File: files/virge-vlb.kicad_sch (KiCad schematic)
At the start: 45 parts, among them J2 VGA, J3 VESA feature, U1 86C325, Y1 14.318MHz

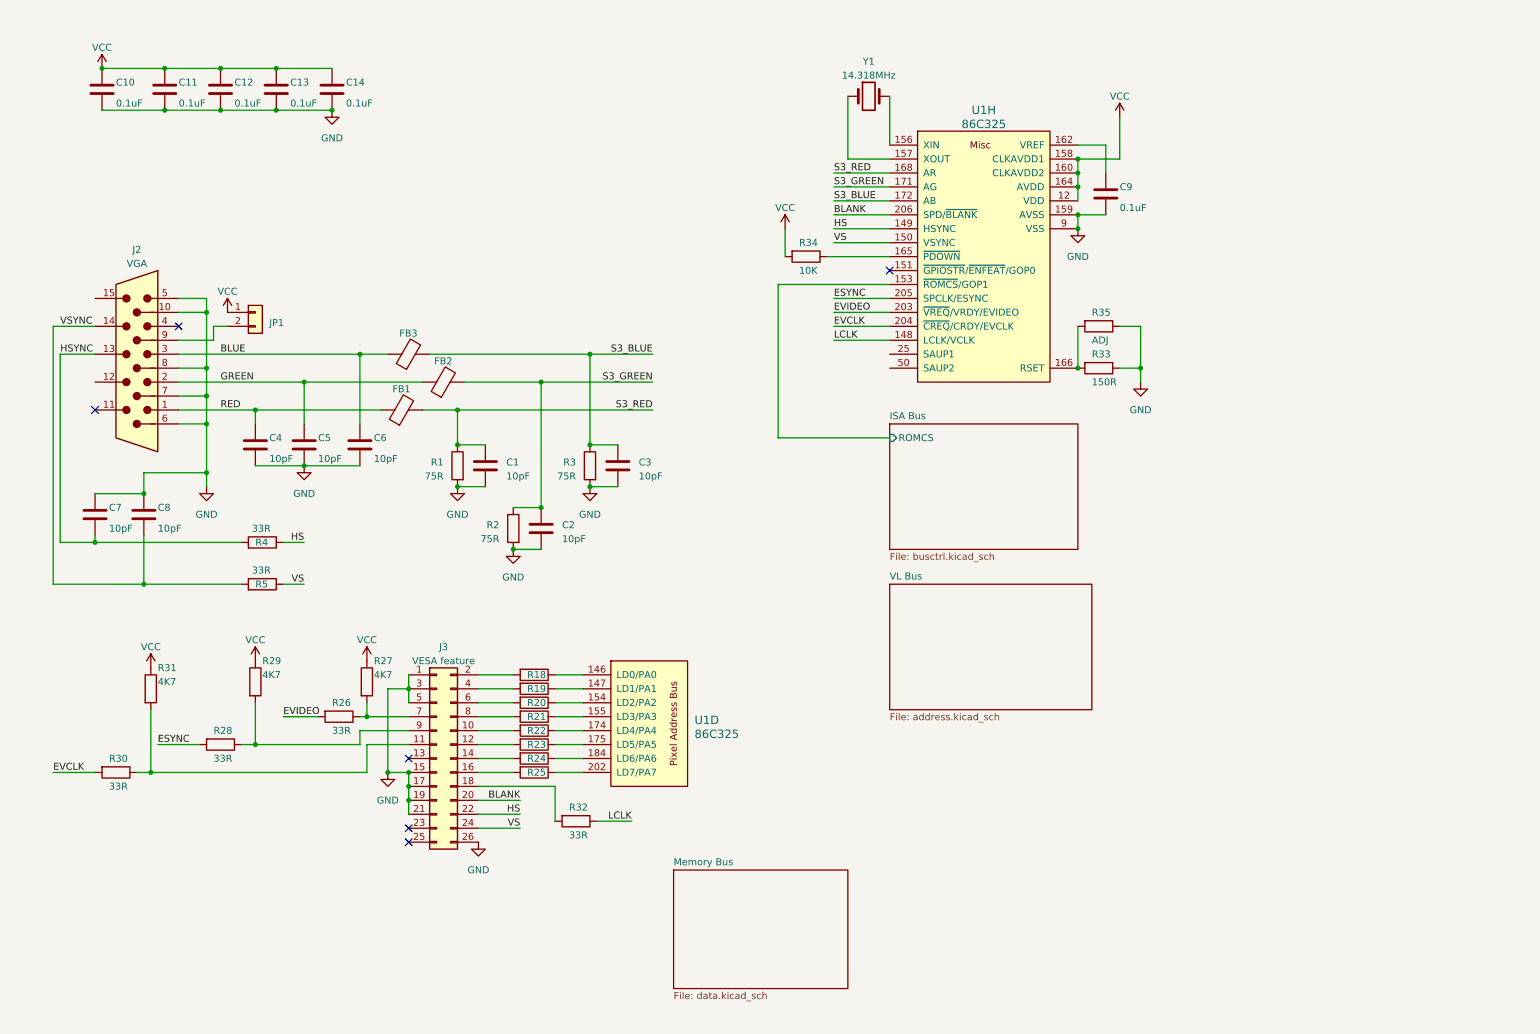
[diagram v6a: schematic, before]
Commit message: added SAUP decoding, adjusted VGA conn.
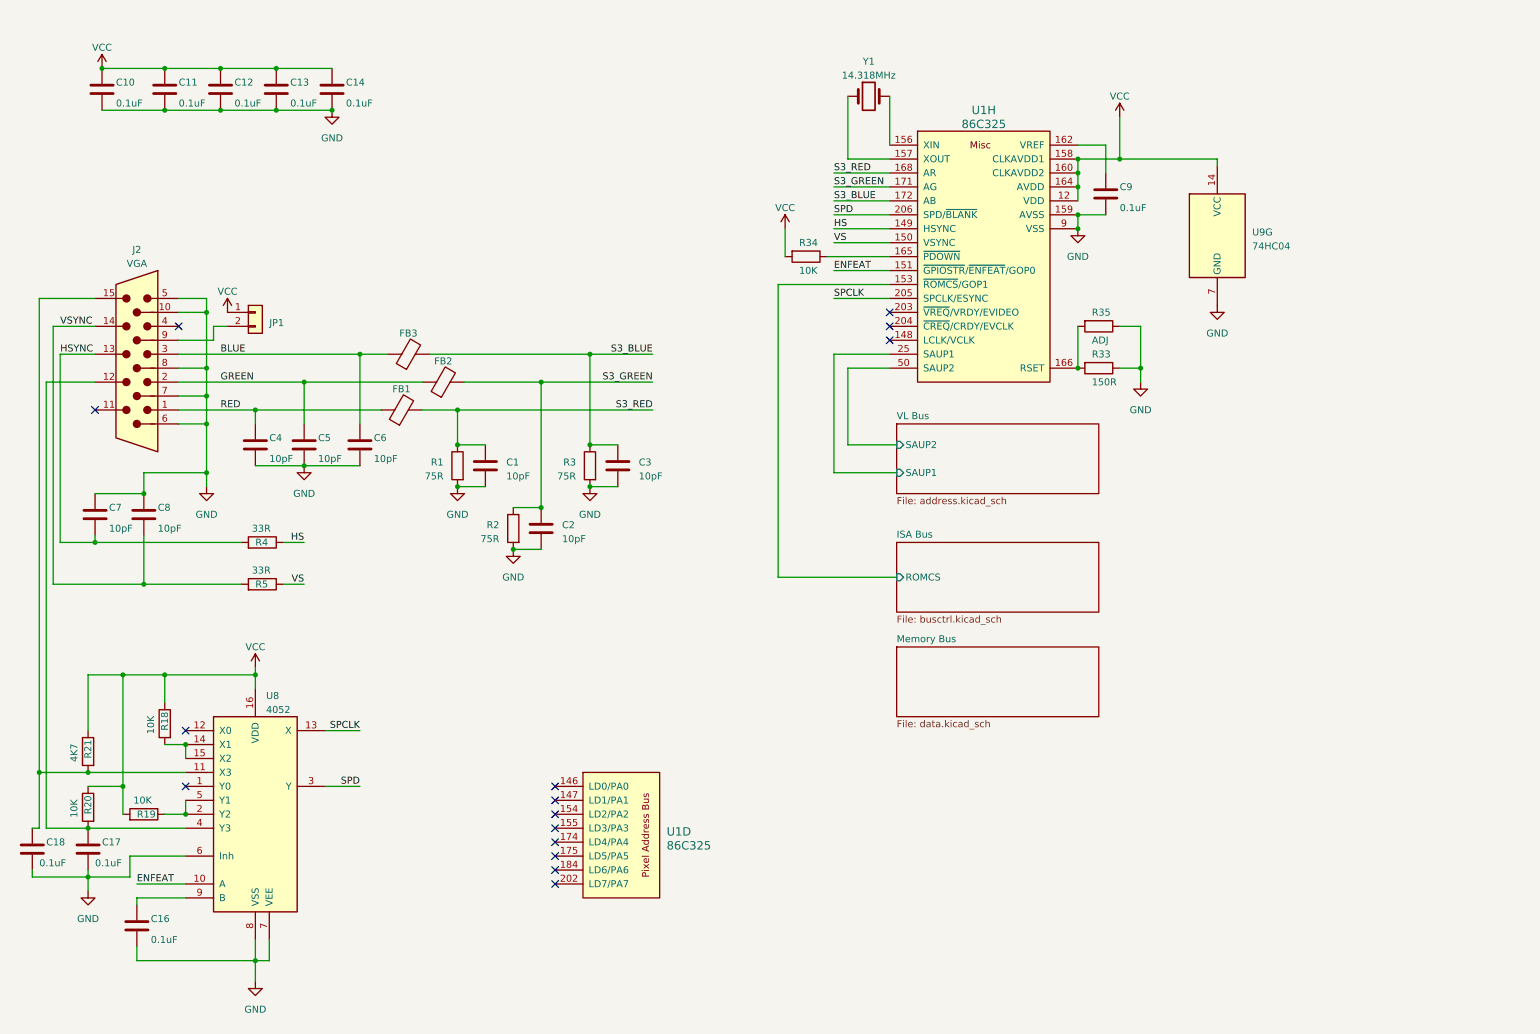
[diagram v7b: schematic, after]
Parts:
- removed J3: VESA feature, Connector_PinHeader_2.54mm:PinHeader_2x13_P2.54mm_Vertical, symbol Connector_Generic:Conn_02x13_Odd_Even
- removed R22, R23, R24, R25, R26, R28, R30, R32: 33R, Resistor_SMD:R_0805_2012Metric_Pad1.20x1.40mm_HandSolder, symbol Device:R
- removed R27, R29, R31: 4K7, Resistor_SMD:R_0805_2012Metric_Pad1.20x1.40mm_HandSolder, symbol Device:R
- added C16, C17, C18: 0.1uF, Capacitor_SMD:C_0805_2012Metric_Pad1.18x1.45mm_HandSolder, symbol Device:C
- added U8: 4052, Package_SO:SO-16_3.9x9.9mm_P1.27mm, symbol 4xxx:4052
- added U9: 74HC04, Package_SO:SO-14_3.9x8.65mm_P1.27mm, symbol 74xx:74HC04
- R18, R19, R20: value 33R -> 10K
- R21: value 33R -> 4K7
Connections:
- net GND: now also C16.2, C17.2, C18.2, U8.6 (Inh), U8.7 (VEE), U8.8 (VSS), U9.7 (GND)
- net VCC: now also R18.1, R19.2, R20.1, R21.1, U8.16 (VDD), U9.14 (VCC)
- net at U1.146 (LD0/PA0): no longer R18.1
- net at U1.147 (LD1/PA1): no longer R19.1
- net at U1.154 (LD2/PA2): no longer R20.1
- net at U1.155 (LD3/PA3): no longer R21.1
- net at R18.2: now also U8.14 (X1), U8.15 (X2)
- net at R20.2: now also J2.12, C17.1, U8.4 (Y3)
- net at R21.2: now also J2.15, C18.1, U8.11 (X3)
- net ENFEAT: now reaches U1.151 (~{GPIOSTR}/~{ENFEAT}/GOP0)
- net ENFEAT: now also U8.10 (A)
- net VL Bus/SAUP1: now reaches U1.25 (SAUP1)
- net VL Bus/SAUP2: now reaches U1.50 (SAUP2)
- net BLANK renamed SPD
- net SPD: now also U8.3 (Y)
- net ESYNC renamed SPCLK
- net SPCLK: now also U8.13 (X)
- net EVCLK: no longer names the net of U1.204 (~{CREQ}/CRDY/EVCLK)
- net EVIDEO: no longer names the net of U1.203 (~{VREQ}/VRDY/EVIDEO)
- net LCLK: no longer names the net of U1.148 (LCLK/VCLK)
- new net: R19.1, U8.2 (Y2), U8.5 (Y1)
- new net: C16.1, U8.9 (B)
- no-connect marks 6 -> 15
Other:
- sheet VL Bus ports: added SAUP1, SAUP2; removed none
- moved on the sheet: U1D

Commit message: added address jumpers
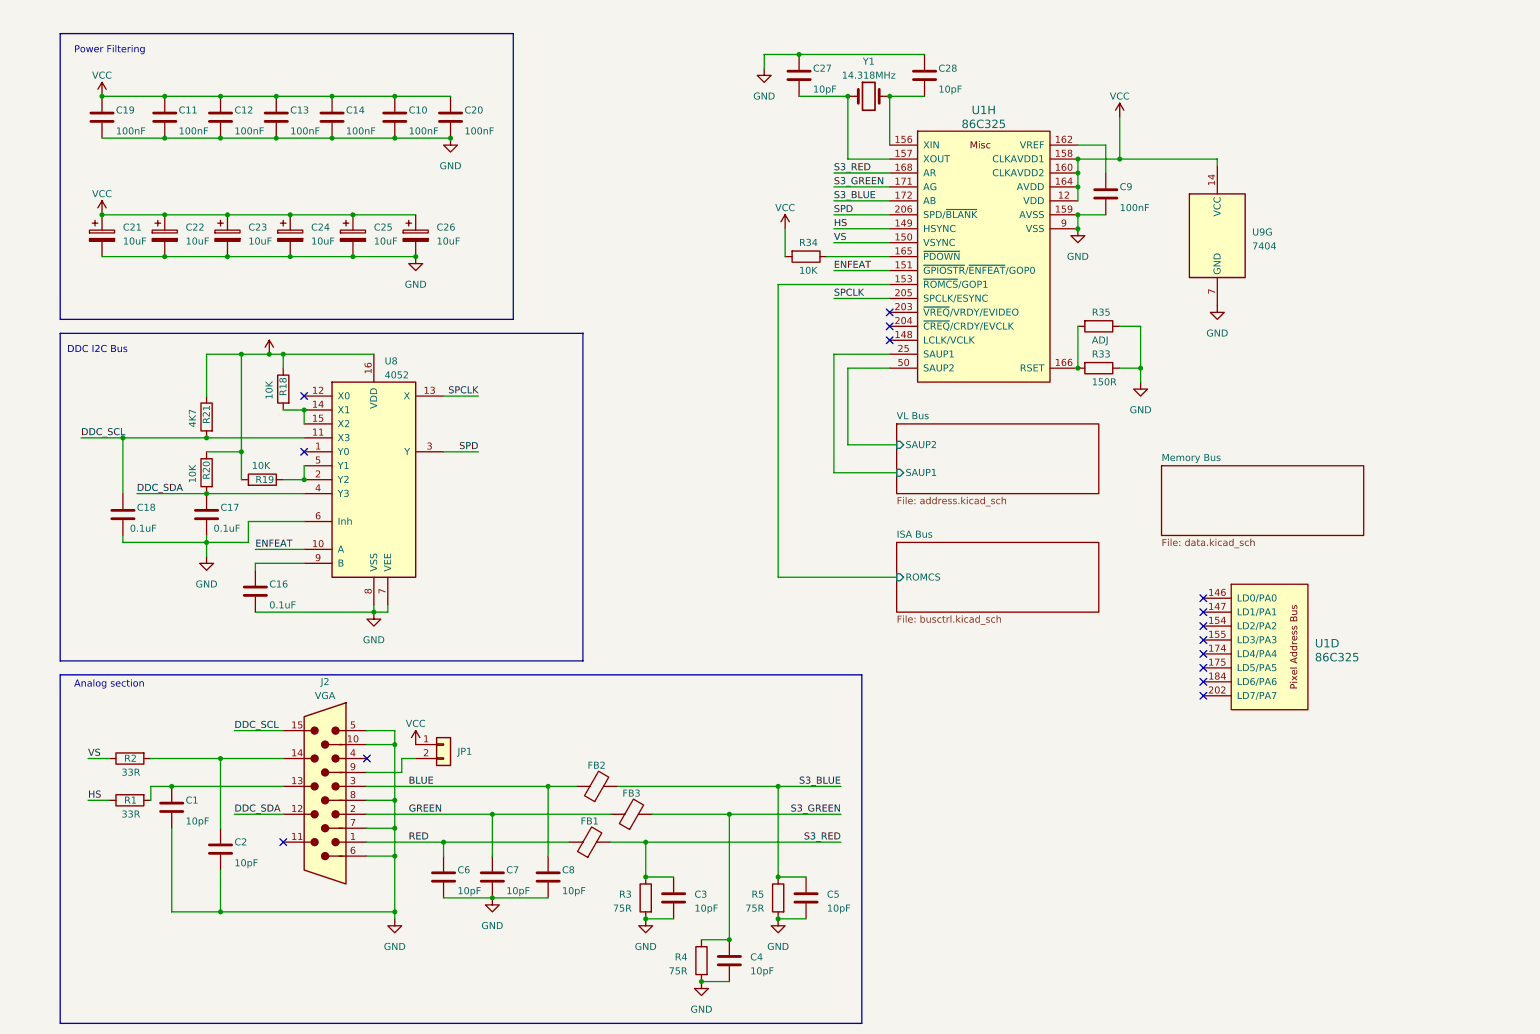
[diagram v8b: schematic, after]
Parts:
- added C10, C20: 100nF, Capacitor_SMD:C_0805_2012Metric_Pad1.18x1.45mm_HandSolder, symbol Device:C
- added C21, C22, C23, C24, C25, C26: 10uF, Capacitor_THT:CP_Radial_D5.0mm_P2.50mm, symbol Device:C_Polarized
- added C27, C28: 10pF, Capacitor_SMD:C_0805_2012Metric_Pad1.18x1.45mm_HandSolder, symbol Device:C
- C11, C12, C13, C14, C9: value 0.1uF -> 100nF
- C19: renamed from C10; value 0.1uF -> 100nF
- R1, R2: value 75R -> 33R
- R4, R5: value 33R -> 75R
- U9: value 74HC04 -> 7404
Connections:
- net BLUE: now also C8.1, FB2.1; no longer C6.1, FB3.1
- net GND: now also C7.2, C8.2, R4.2, R5.2, C10.2, C20.2, C21.2, C22.2, C23.2, C24.2, C25.2, C26.2, C27.1, C28.1; no longer C7.1, C8.1, R1.2, R2.2
- net GREEN: now also C7.1, FB3.1; no longer C5.1, FB2.1
- net HS: now also R1.1; no longer R4.1
- net RED: now also C6.1; no longer C4.1
- net S3_BLUE: now also C5.1, FB2.2, R5.1; no longer C3.1, FB3.2, R3.1
- net S3_GREEN: now also C4.1, FB3.2, R4.1; no longer C2.1, FB2.2, R2.1
- net S3_RED: now also C3.1, R3.1; no longer C1.1, R1.1
- net VCC: now also C10.1, C20.1, C21.1, C22.1, C23.1, C24.1, C25.1, C26.1
- net VS: now also R2.1; no longer R5.1
- net DDC_SCL: now reaches C18.1, J2.15, R21.2, U8.11 (X3)
- net DDC_SDA: now reaches C17.1, J2.12, R20.2, U8.4 (Y3)
- net at U1.156 (XIN), Y1.2: now also C28.2
- net at U1.157 (XOUT), Y1.1: now also C27.2
- removed net HSYNC: C7.2, J2.13, R4.2
- removed net VSYNC: C8.2, J2.14, R5.2
- new net: C2.1, J2.14, R2.2
- new net: C1.1, J2.13, R1.2
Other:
- note added: "Analog section"
- note added: "DDC I2C Bus"
- note added: "Power Filtering"
- moved on the sheet: C11, C12, C13, C14, C16, C17, C18, C19, R18, R19, R20, R21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
